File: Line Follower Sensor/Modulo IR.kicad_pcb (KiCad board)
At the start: 2 copper layers, 17.3 x 32.5 mm, 13 parts, among them U1 LM358N, U10 100nF, U12 TCRT5000, U13 100R, U3 1K, U5 20K, U6 10K, U7 10k, U8 CON3_ET, U9 LED

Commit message: potenciometro cambiado
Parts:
- removed G***: LOGO, logos_frizzy:logo_lf
- U7: footprint Potentiometers:Potentiometer_Trimmer-Suntan-TSR-3386P -> Potentiometers:Potentiometer_Trimmer_Bourns_3296W
- moved U9 13.9 mm to (146.8, 89.2), turned to 270 degrees
- moved U7 5.74 mm to (150.6, 94.0)
- moved U13 5.09 mm to (159.5, 86.4)
- moved U12 3.94 mm to (153.4, 86.6)
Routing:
- net GNDREF: track 25.5 -> 7.57 mm
- net Net-(U3-Pad1): track 3.03 -> 15.0 mm, vias 0 -> 2
- net VCC: track 50.0 -> 60.8 mm, vias 2 -> 4
- net A0: track 30.6 -> 26.9 mm
- net Net-(U6-Pad1): track 9.73 -> 7.73 mm
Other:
- board size 17.3 x 32.5 mm -> 17.3 x 29.2 mm

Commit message: Logo atom cambiado
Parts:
- added G***: LOGO, Grape:atom_small, B.Cu at (158.6, 107.3)
- added G***: LOGO, logos_frizzy:web, B.Cu at (146.7, 89.4)

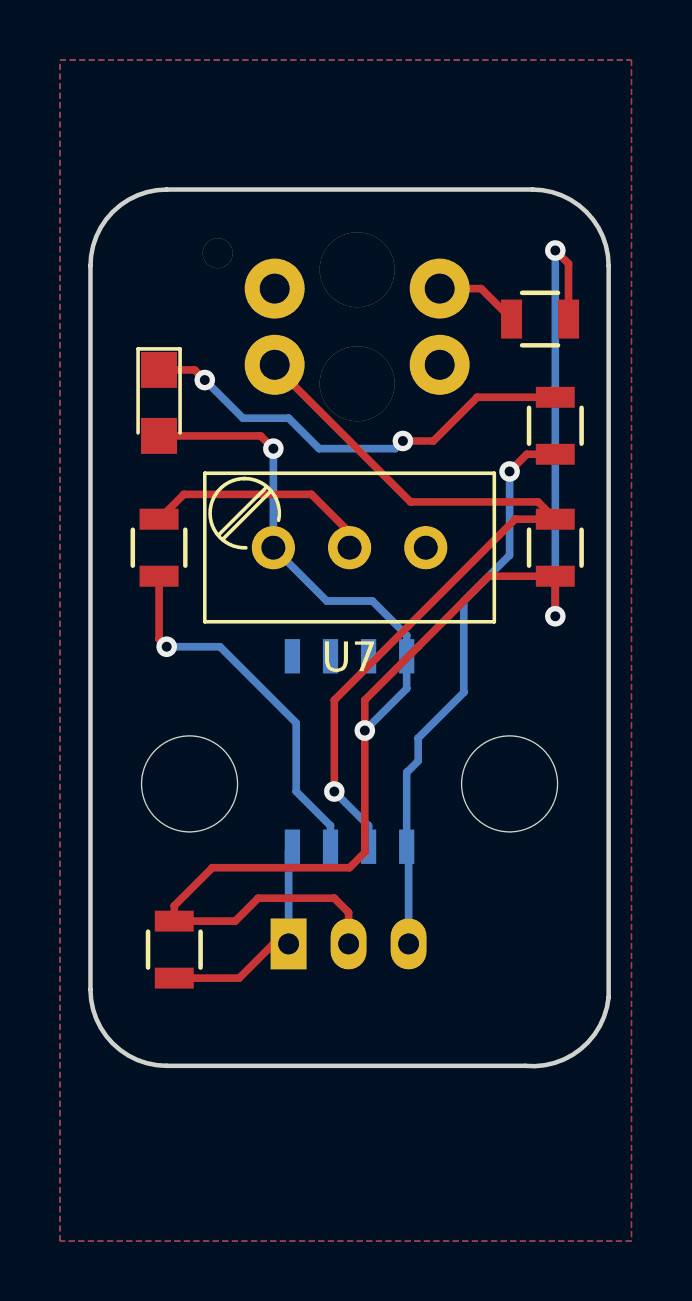
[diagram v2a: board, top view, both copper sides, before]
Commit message: conector cambiado
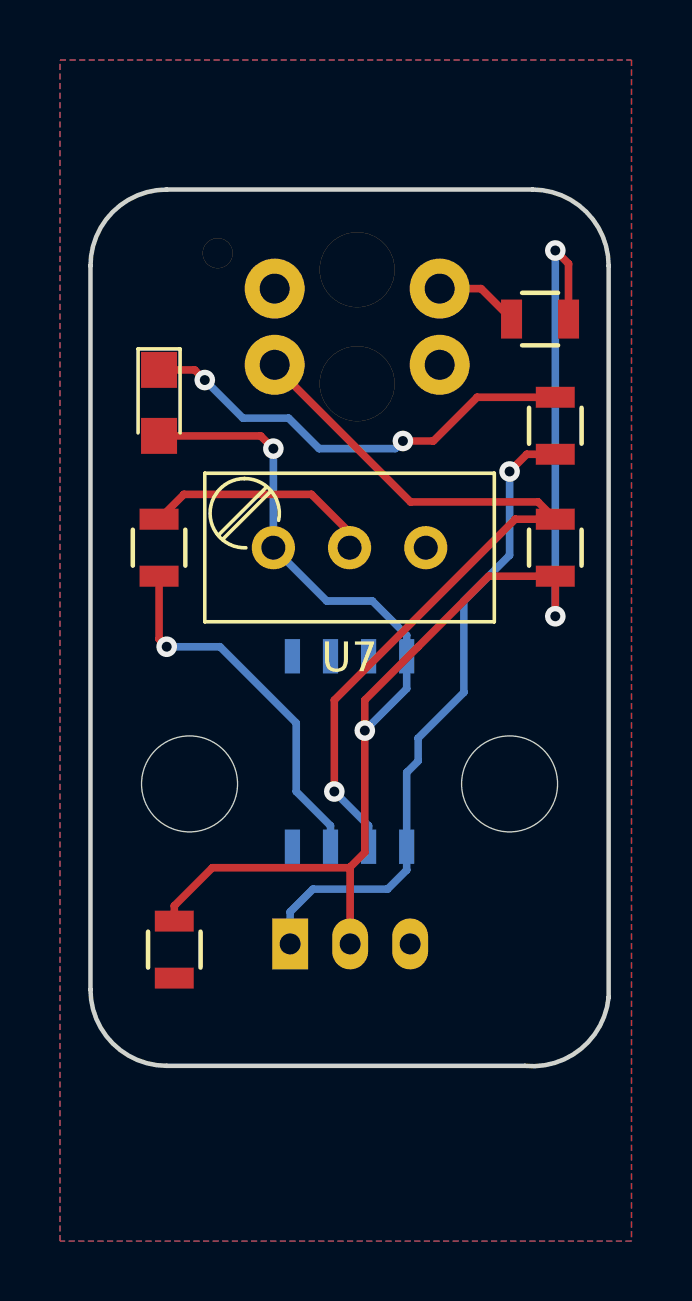
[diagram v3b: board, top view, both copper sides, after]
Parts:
- moved U8 0.05 mm to (151.2, 107.2)
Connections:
- U8 pad 1: GNDREF -> Net-(U1-Pad1)
- U8 pad 3: Net-(U1-Pad1) -> GNDREF
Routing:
- net GNDREF: track 7.57 -> 0.18 mm
- net VCC: track 60.8 -> 56.0 mm
- net Net-(U1-Pad1): track 19.0 -> 22.1 mm
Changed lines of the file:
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@@
     (area 144.450999 81.966999 161.873001 111.339669)
     (thickness 1.6)
-    (drawings 10)
-    (tracks 85)
+    (drawings 11)
+    (tracks 82)
     (zones 0)
     (modules 14)
@@
   )
   (module Connectors_JST:JST_PH_S3B-PH-K_03x2.00mm_Angled (layer F.Cu)
-    (at 151.13 107.188)
+    (at 151.1808 107.188)
     (descr http://www.jst-mfg.com/product/pdf/eng/ePH.pdf)
     (tags "connector jst ph")
@@
     (fp_line (start 6.45 6.75) (end -2.45 6.75) (layer Dwgs.User) (width 0.05))
     (pad 1 thru_hole rect (at 0 0) (size 1.2 1.7) (drill 0.7) (layers *.Cu *.Mask)
-      (net 2 GNDREF))
+      (net 5 "Net-(U1-Pad1)"))
     (pad 2 thru_hole oval (at 2 0) (size 1.2 1.7) (drill 0.7) (layers *.Cu *.Mask)
       (net 1 VCC))
     (pad 3 thru_hole oval (at 4 0) (size 1.2 1.7) (drill 0.7) (layers *.Cu *.Mask)
-      (net 5 "Net-(U1-Pad1)"))
+      (net 2 GNDREF))
     (model ../../../../../home/david/Escritorio/hola/walter/conn_jst-ph/s3b-ph-kl.wrl
       (at (xyz 0.08 0 0))
@@
       (xy -3.05495 1.225397) (xy -3.006513 1.238605) (xy -2.963342 1.241237) (xy -2.923536 1.239758)) (layer B.SilkS) (width 0.01))
   )
+  (gr_line (start 163.2712 105.8164) (end 149.1996 105.8164) (angle 90) (layer Dwgs.User) (width 0.2))
   (gr_line (start 144.526 84.582) (end 144.526 108.712) (angle 90) (layer Edge.Cuts) (width 0.15))
   (gr_line (start 161.798 108.966) (end 161.798 84.582) (angle 90) (layer Edge.Cuts) (width 0.15))
@@
   (gr_arc (start 159.258 108.712) (end 161.798 108.966) (angle 90) (layer Edge.Cuts) (width 0.15))
   (gr_arc (start 159.258 84.582) (end 159.258 82.042) (angle 90) (layer Edge.Cuts) (width 0.15))
+  (segment (start 153.1808 107.188) (end 153.1808 104.6292) (width 0.254) (layer F.Cu) (net 1) (status 400000))
+  (segment (start 153.1808 104.6292) (end 153.162 104.648) (width 0.254) (layer F.Cu) (net 1))
   (segment (start 160.02 94.93) (end 160.02 96.266) (width 0.254) (layer F.Cu) (net 1))
   (segment (start 160.462 84.516) (end 160.462 86.36) (width 0.254) (layer F.Cu) (net 1))
@@
   (segment (start 148.59 104.648) (end 153.162 104.648) (width 0.254) (layer F.Cu) (net 1))
   (segment (start 147.32 105.918) (end 148.59 104.648) (width 0.254) (layer F.Cu) (net 1))
-  (segment (start 147.32 106.4285) (end 149.3495 106.4285) (width 0.254) (layer F.Cu) (net 1))
-  (segment (start 153.13 106.14) (end 153.13 107.188) (width 0.254) (layer F.Cu) (net 1))
-  (segment (start 152.654 105.664) (end 153.13 106.14) (width 0.254) (layer F.Cu) (net 1))
-  (segment (start 150.114 105.664) (end 152.654 105.664) (width 0.254) (layer F.Cu) (net 1))
-  (segment (start 149.3495 106.4285) (end 150.114 105.664) (width 0.254) (layer F.Cu) (net 1))
-  (segment (start 151.13 107.188) (end 151.13 104.0765) (width 0.254) (layer B.Cu) (net 2))
   (segment (start 151.13 104.0765) (end 151.257 103.9495) (width 0.254) (layer B.Cu) (net 2))
-  (segment (start 147.32 108.3285) (end 149.4815 108.3285) (width 0.254) (layer F.Cu) (net 2))
-  (segment (start 149.4815 108.3285) (end 150.622 107.188) (width 0.254) (layer F.Cu) (net 2))
-  (segment (start 150.622 107.188) (end 151.13 107.188) (width 0.254) (layer F.Cu) (net 2))
   (segment (start 152.527 103.9495) (end 152.527 103.251) (width 0.254) (layer B.Cu) (net 3))
   (segment (start 146.812 97.028) (end 146.812 94.93) (width 0.254) (layer F.Cu) (net 3))
@@
   (segment (start 159.446 92.456) (end 160.02 93.03) (width 0.254) (layer F.Cu) (net 4))
   (segment (start 153.67 103.8225) (end 153.797 103.9495) (width 0.254) (layer B.Cu) (net 4))
+  (segment (start 151.1808 107.188) (end 151.1808 106.1212) (width 0.254) (layer B.Cu) (net 5) (status 400000))
+  (segment (start 155.067 104.7242) (end 155.067 103.9495) (width 0.254) (layer B.Cu) (net 5) (status 800000))
+  (segment (start 154.432 105.3592) (end 155.067 104.7242) (width 0.254) (layer B.Cu) (net 5))
+  (segment (start 151.9428 105.3592) (end 154.432 105.3592) (width 0.254) (layer B.Cu) (net 5))
+  (segment (start 151.1808 106.1212) (end 151.9428 105.3592) (width 0.254) (layer B.Cu) (net 5))
   (segment (start 155.067 103.9495) (end 155.067 101.473) (width 0.254) (layer B.Cu) (net 5))
   (segment (start 159.07 90.866) (end 160.02 90.866) (width 0.254) (layer F.Cu) (net 5))
   (segment (start 155.067 101.473) (end 155.448 101.092) (width 0.254) (layer B.Cu) (net 5))
-  (segment (start 155.13 107.188) (end 155.13 104.0125) (width 0.254) (layer B.Cu) (net 5))
   (segment (start 155.13 104.0125) (end 155.067 103.9495) (width 0.254) (layer B.Cu) (net 5))
   (segment (start 158.496 91.44) (end 159.07 90.866) (width 0.254) (layer F.Cu) (net 5))

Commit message: Referencia del potenciometro eliminada
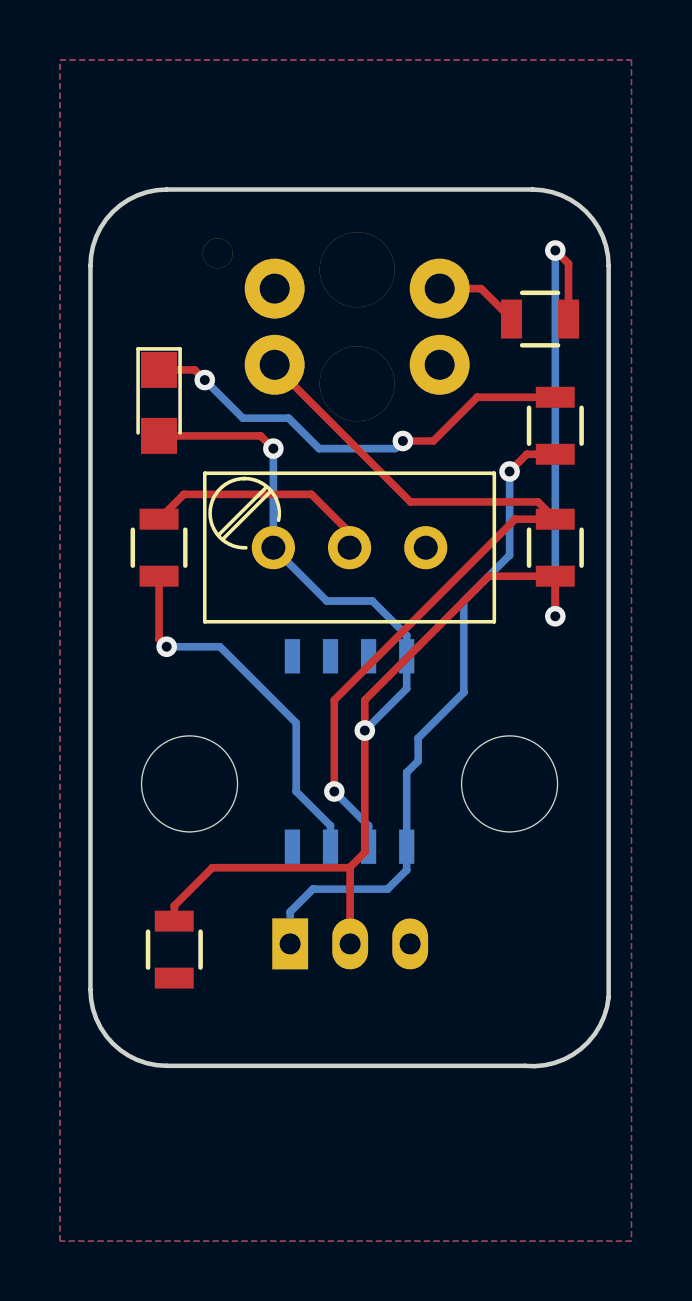
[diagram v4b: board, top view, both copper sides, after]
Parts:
- moved G*** 0.22 mm to (158.8, 107.5), turned to 180 degrees
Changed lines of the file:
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@@
     (descr "Spindle Trimmer Potentiometer, Bourns 3296W, https://www.bourns.com/pdfs/3296.pdf")
     (tags "Spindle Trimmer Potentiometer   Bourns 3296W")
-    (fp_text reference U7 (at -2.54 -3.66 180) (layer F.SilkS)
-      (effects (font (size 1 1) (thickness 0.15)))
-    )
-    (fp_text value 10k (at -2.54 3.67 180) (layer F.Fab)
+    (fp_text reference U7 (at -2.54 -3.66 180) (layer F.SilkS) hide
+      (effects (font (size 1 1) (thickness 0.15)))
+    )
+    (fp_text value 10k (at -2.54 3.67 180) (layer F.Fab) hide
       (effects (font (size 1 1) (thickness 0.15)))
     )
@@
   )
   (module Grape:atom_small (layer B.Cu)
-    (at 158.623 107.315)
-    (fp_text reference G*** (at 0 0) (layer B.SilkS) hide
+    (at 158.7881 107.4674 180)
+    (fp_text reference G*** (at 0 0 180) (layer B.SilkS) hide
       (effects (font (thickness 0.3)) (justify mirror))
     )
-    (fp_text value LOGO (at 0.75 0) (layer B.SilkS) hide
+    (fp_text value LOGO (at 0.75 0 180) (layer B.SilkS) hide
       (effects (font (thickness 0.3)) (justify mirror))
     )
@@
       (xy -3.05495 1.225397) (xy -3.006513 1.238605) (xy -2.963342 1.241237) (xy -2.923536 1.239758)) (layer B.SilkS) (width 0.01))
   )
+  (gr_line (start 147.066 111.252) (end 159.004 111.252) (angle 90) (layer Edge.Cuts) (width 0.15))
+  (gr_line (start 147.066 82.042) (end 159.258 82.042) (angle 90) (layer Edge.Cuts) (width 0.15))
   (gr_line (start 163.2712 105.8164) (end 149.1996 105.8164) (angle 90) (layer Dwgs.User) (width 0.2))
+  (gr_arc (start 159.258 108.712) (end 161.798 108.966) (angle 90) (layer Edge.Cuts) (width 0.15))
   (gr_line (start 144.526 84.582) (end 144.526 108.712) (angle 90) (layer Edge.Cuts) (width 0.15))
   (gr_line (start 161.798 108.966) (end 161.798 84.582) (angle 90) (layer Edge.Cuts) (width 0.15))
@@
     (arrow2b (pts (xy 167.132 78.74) (xy 167.718421 79.866504)))
   )
-  (gr_line (start 147.066 82.042) (end 159.258 82.042) (angle 90) (layer Edge.Cuts) (width 0.15))
   (gr_arc (start 147.066 84.582) (end 144.526 84.582) (angle 90) (layer Edge.Cuts) (width 0.15))
-  (gr_line (start 147.066 111.252) (end 159.004 111.252) (angle 90) (layer Edge.Cuts) (width 0.15))
   (gr_arc (start 147.066 108.712) (end 147.066 111.252) (angle 90) (layer Edge.Cuts) (width 0.15))
-  (gr_arc (start 159.258 108.712) (end 161.798 108.966) (angle 90) (layer Edge.Cuts) (width 0.15))
   (gr_arc (start 159.258 84.582) (end 159.258 82.042) (angle 90) (layer Edge.Cuts) (width 0.15))
-  (segment (start 153.1808 107.188) (end 153.1808 104.6292) (width 0.254) (layer F.Cu) (net 1) (status 400000))
+  (segment (start 153.1808 107.188) (end 153.1808 104.6292) (width 0.254) (layer F.Cu) (net 1))
   (segment (start 153.1808 104.6292) (end 153.162 104.648) (width 0.254) (layer F.Cu) (net 1))
   (segment (start 160.02 94.93) (end 160.02 96.266) (width 0.254) (layer F.Cu) (net 1))
@@
   (segment (start 159.446 92.456) (end 160.02 93.03) (width 0.254) (layer F.Cu) (net 4))
   (segment (start 153.67 103.8225) (end 153.797 103.9495) (width 0.254) (layer B.Cu) (net 4))
-  (segment (start 151.1808 107.188) (end 151.1808 106.1212) (width 0.254) (layer B.Cu) (net 5) (status 400000))
-  (segment (start 155.067 104.7242) (end 155.067 103.9495) (width 0.254) (layer B.Cu) (net 5) (status 800000))
+  (segment (start 151.1808 107.188) (end 151.1808 106.1212) (width 0.254) (layer B.Cu) (net 5))
+  (segment (start 155.067 104.7242) (end 155.067 103.9495) (width 0.254) (layer B.Cu) (net 5))
   (segment (start 154.432 105.3592) (end 155.067 104.7242) (width 0.254) (layer B.Cu) (net 5))
   (segment (start 151.9428 105.3592) (end 154.432 105.3592) (width 0.254) (layer B.Cu) (net 5))
